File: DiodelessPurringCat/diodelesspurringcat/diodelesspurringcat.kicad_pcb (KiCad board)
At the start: 2 copper layers, 114 x 92.4 mm, 21 parts, among them J1 ScreenL, U1 ProMicro-kbd

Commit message: trying to make a reversible nice view
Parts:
- 0/9, 1/8, 10/19, 11/18, 12/17, 13/16, 14/15, 2/7, 20/25, 21/24, 22/23, 26/29, 27/28, 3/6, 4/5: footprint keyswitches:Kailh_socket_PG1350_reversible -> chelming-kbd:choc_v1_hotswap_reversible_no_extras
- J1: value ScreenL -> nice!view; footprint Connector_PinHeader_2.54mm:PinHeader_1x05_P2.54mm_Vertical -> chelming-kbd:nice-view_reversible
- moved RSW1 43.4 mm to (199.0, 85.0)
- moved J1 17.3 mm to (238.8, 65.7), turned to 0 degrees
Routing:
- net CS: track 62.3 -> 0.00 mm
- net s27: track 38.8 -> 0.00 mm, vias 1 -> 0
- net s26: track 54.7 -> 26.2 mm
- net MOSI: track 27.4 -> 0.00 mm
- net SCK: track 23.8 -> 0.00 mm
- net (no net): track 0.00 -> 3.74 mm

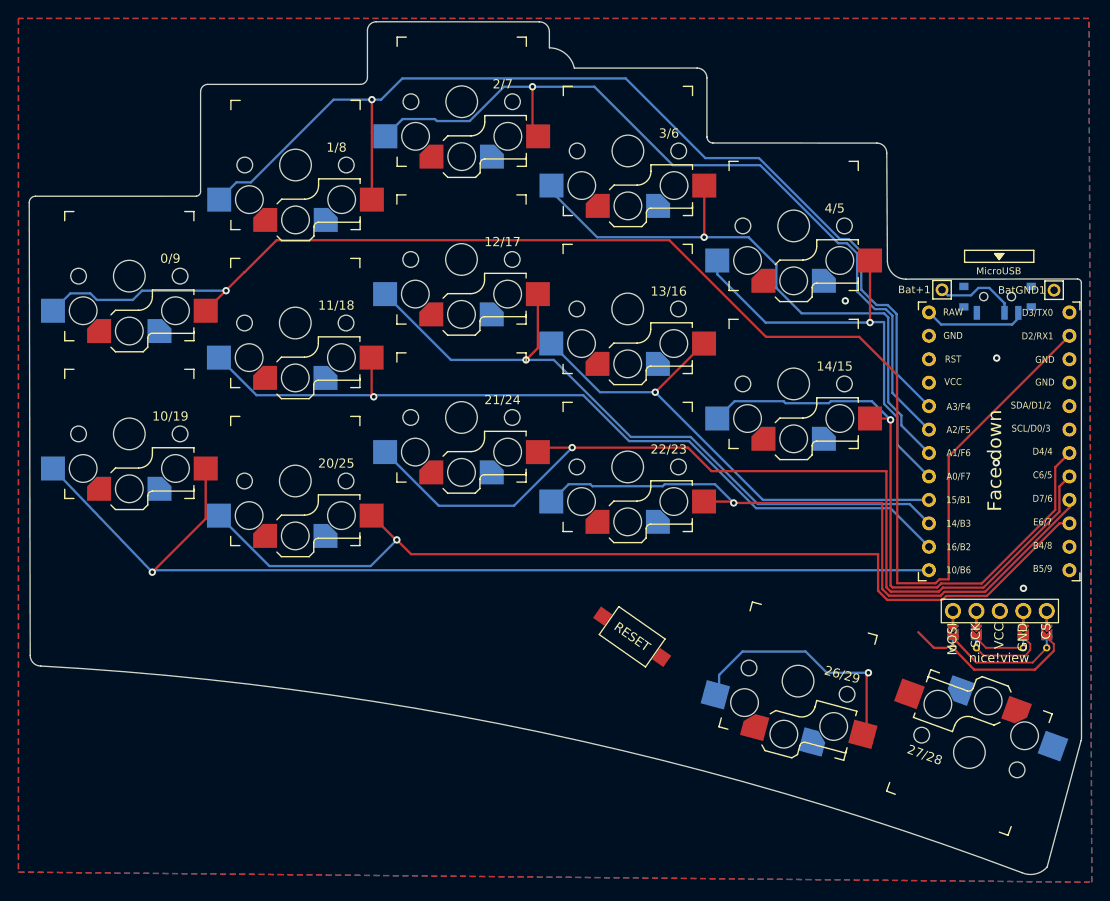
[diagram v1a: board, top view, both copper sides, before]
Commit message: moving back to reversible. still diodeless. needs case mounts
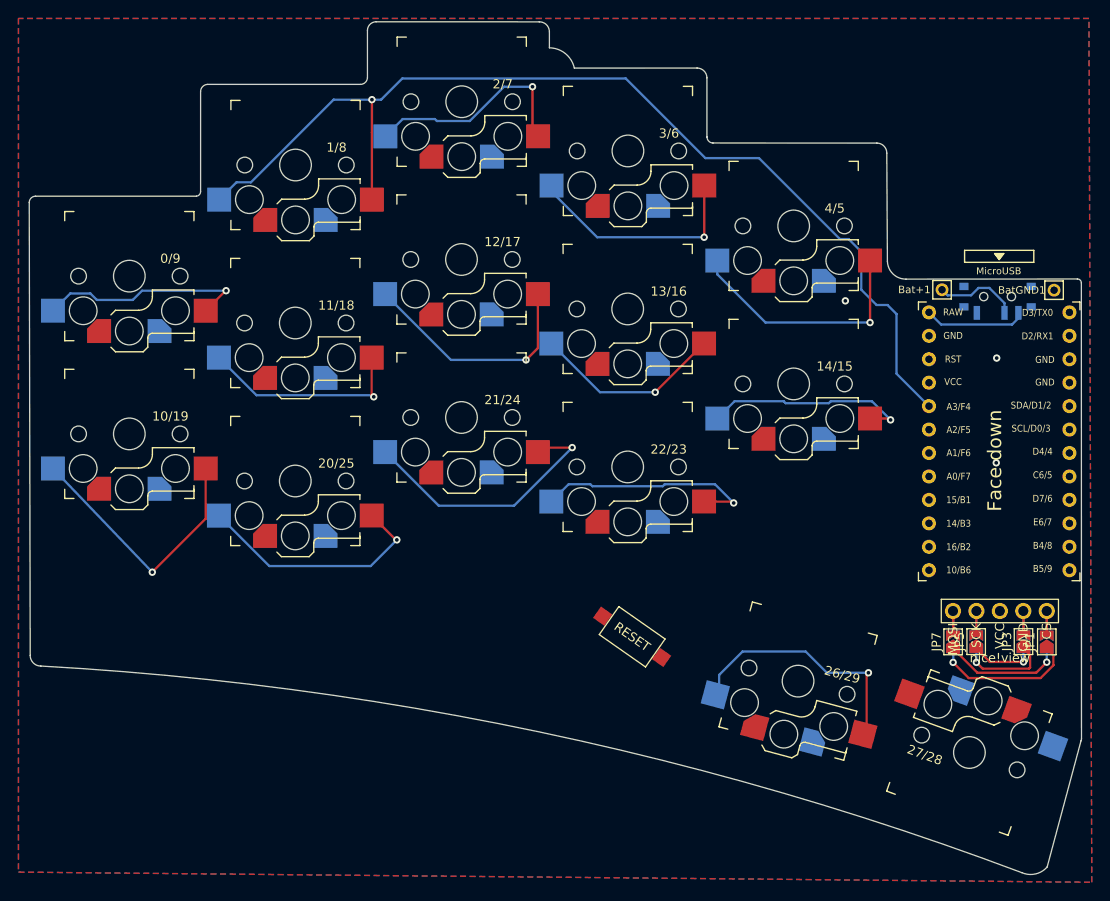
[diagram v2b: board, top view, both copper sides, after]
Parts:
- added JP0: Jumper_2_Small_Open, Jumper:SolderJumper-2_P1.3mm_Open_TrianglePad1.0x1.5mm, B.Cu at (233.8, 85.5)
- added JP1: Jumper_2_Small_Open, Jumper:SolderJumper-2_P1.3mm_Open_TrianglePad1.0x1.5mm, F.Cu at (243.9, 85.5)
- added JP2: Jumper_2_Small_Open, Jumper:SolderJumper-2_P1.3mm_Open_TrianglePad1.0x1.5mm, B.Cu at (236.3, 85.5)
- added JP3: Jumper_2_Small_Open, Jumper:SolderJumper-2_P1.3mm_Open_TrianglePad1.0x1.5mm, F.Cu at (241.4, 85.5)
- added JP4: Jumper_2_Small_Open, Jumper:SolderJumper-2_P1.3mm_Open_TrianglePad1.0x1.5mm, B.Cu at (241.4, 85.5)
- added JP5: Jumper_2_Small_Open, Jumper:SolderJumper-2_P1.3mm_Open_TrianglePad1.0x1.5mm, F.Cu at (236.3, 85.5)
- added JP6: Jumper_2_Small_Open, Jumper:SolderJumper-2_P1.3mm_Open_TrianglePad1.0x1.5mm, B.Cu at (243.9, 85.6)
- added JP7: Jumper_2_Small_Open, Jumper:SolderJumper-2_P1.3mm_Open_TrianglePad1.0x1.5mm, F.Cu at (233.8, 85.5)
- J1: footprint chelming-kbd:nice-view_reversible -> nice_view:nice_view
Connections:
- J1 pad 1: MOSI -> NV1
- J1 pad 2: SCK -> NV2
- J1 pad 4: gnd -> NV4
- J1 pad 5: CS -> NV5
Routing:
- net s0: track 164.5 -> 23.4 mm
- net s10: track 113.4 -> 29.2 mm
- net s20: track 107.9 -> 26.5 mm
- net s21: track 103.7 -> 29.2 mm
- net s11: track 89.9 -> 22.9 mm
- net s2: track 89.6 -> 24.0 mm
- net s12: track 76.9 -> 25.9 mm
- net s22: track 75.6 -> 24.8 mm
- net s14: track 69.0 -> 22.9 mm
- net s3: track 66.4 -> 24.8 mm
- net s13: track 55.4 -> 20.9 mm
- net s4: track 47.2 -> 26.9 mm
- net MOSI: track 0.00 -> 15.8 mm, vias 0 -> 1
- net CS: track 0.00 -> 13.2 mm, vias 0 -> 1
- net SCK: track 0.00 -> 10.0 mm, vias 0 -> 1
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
